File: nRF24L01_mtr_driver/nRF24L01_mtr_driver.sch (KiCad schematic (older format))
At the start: 135 parts, among them J1 Micro USB, J2 I/O, J4 VBAT, J5 MTR, J6 SERVO, J7 ICSP, Q1 AO4484, Q2 AO4484, Q3 AO4484, Q4 AO4484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

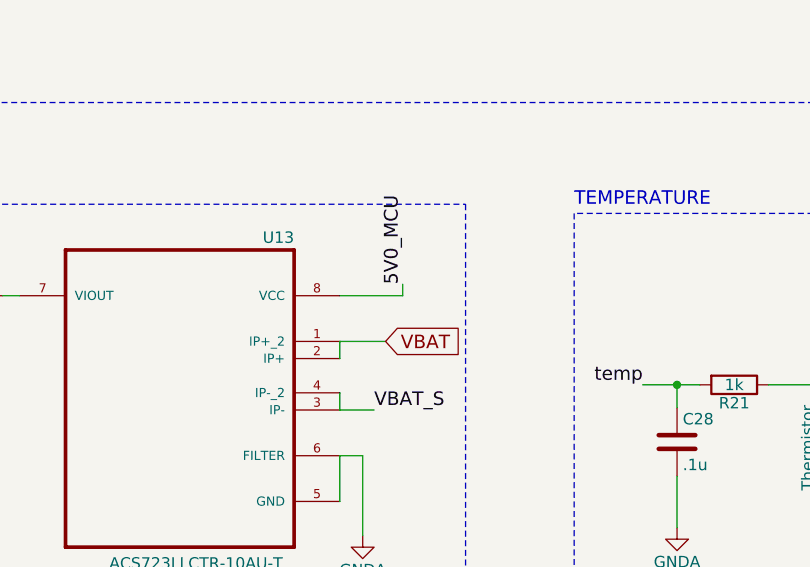
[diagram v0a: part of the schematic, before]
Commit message: 23 components left, stil needs routing
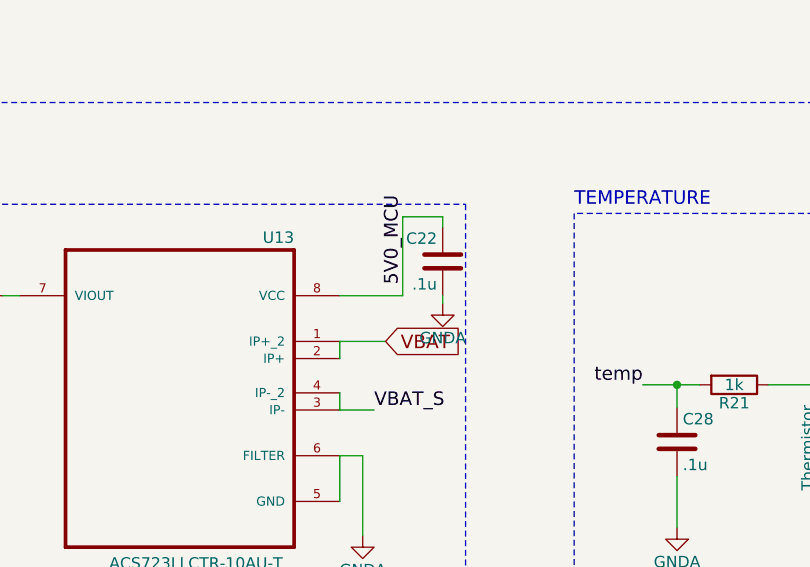
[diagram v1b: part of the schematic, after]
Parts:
- added C22: .1u, Capacitors_SMD:C_0402, symbol C
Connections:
- net 5V0_MCU: now also C22.1
- net GNDA: now also C22.2
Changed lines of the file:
@@
 	22630 9335 22630 8985
 Wire Wire Line
-	22805 8285 22805 8235
-Wire Wire Line
-	22530 8285 22805 8285
+	22805 7940 22805 8285
+Wire Wire Line
+	22805 8285 22530 8285
 Wire Wire Line
 	20590 12520 20665 12520
@@
 Text Notes 3750 6575 0    59   ~ 0
 F3542CT-ND
+$Comp
+L C C22
+U 1 1 5C739D0E
+P 22980 8135
+F 0 "C22" H 23005 8235 50  0000 L CNN
+F 1 ".1u" H 23005 8035 50  0000 L CNN
+F 2 "Capacitors_SMD:C_0402" H 23018 7985 50  0001 C CNN
+F 3 "" H 22980 8135 50  0001 C CNN
+	1    22980 8135
+	-1   0    0    -1
+$EndComp
+$Comp
+L GNDA #PWR081
+U 1 1 5C739D9E
+P 22980 8320
+F 0 "#PWR081" H 22980 8070 50  0001 C CNN
+F 1 "GNDA" H 22980 8170 50  0000 C CNN
+F 2 "" H 22980 8320 50  0001 C CNN
+F 3 "" H 22980 8320 50  0001 C CNN
+	1    22980 8320
+	-1   0    0    -1
+$EndComp
+Wire Wire Line
+	22980 8285 22980 8320
+Wire Wire Line
+	22805 7940 22980 7940
+Wire Wire Line
+	22980 7940 22980 7985
 $EndSCHEMATC

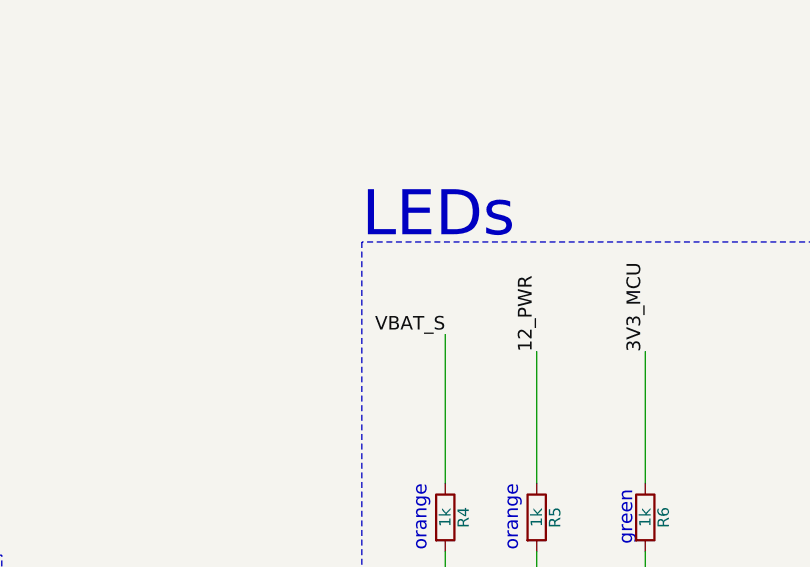
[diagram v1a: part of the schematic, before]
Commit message: arranged silkscreen, started rounting (ftdi)
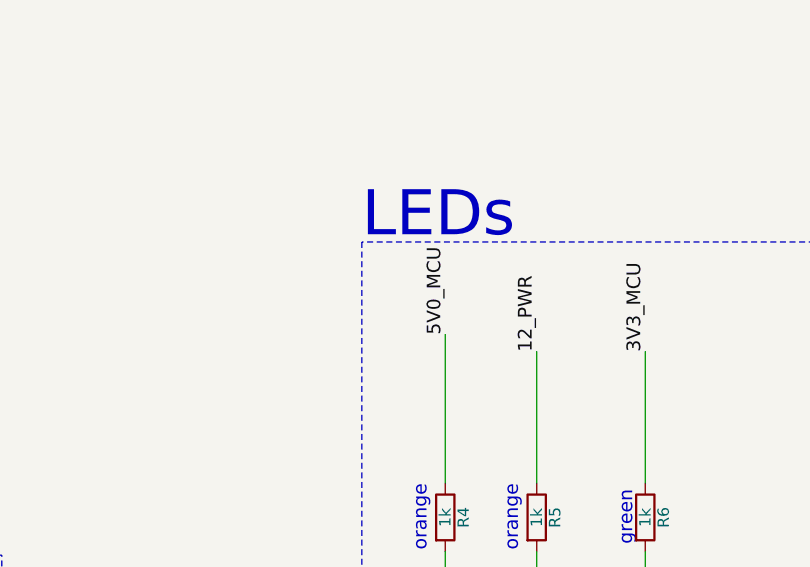
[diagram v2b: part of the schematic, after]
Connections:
- net 5V0_MCU: now also R4.1
- net VBAT_S: no longer R4.1
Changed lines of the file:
@@
 Text Label 9405 16400 1    60   ~ 0
 5V0_MCU
-Text Label 21735 2710 2    59   ~ 0
-VBAT_S
+Text Label 21735 2710 1    59   ~ 0
+5V0_MCU
 $Comp
 L LED D7

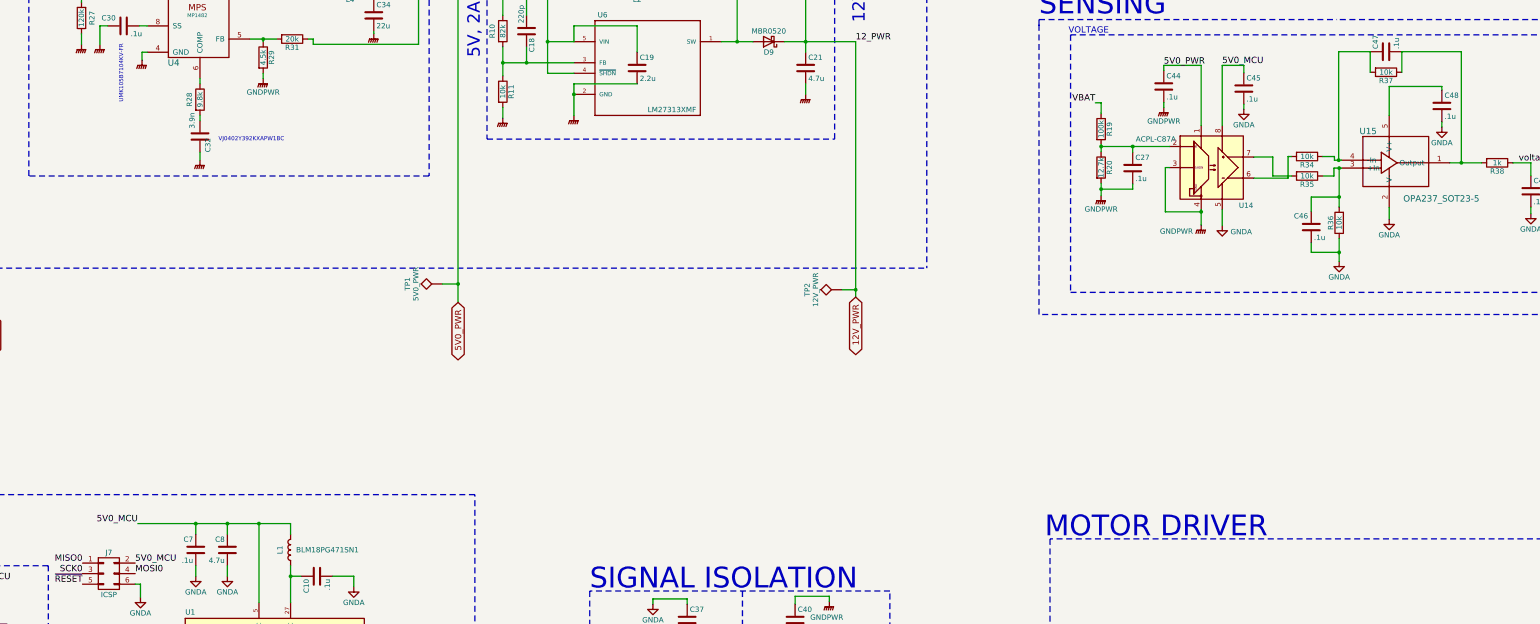
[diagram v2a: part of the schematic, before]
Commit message: ready for 2 or 4 layer implementation
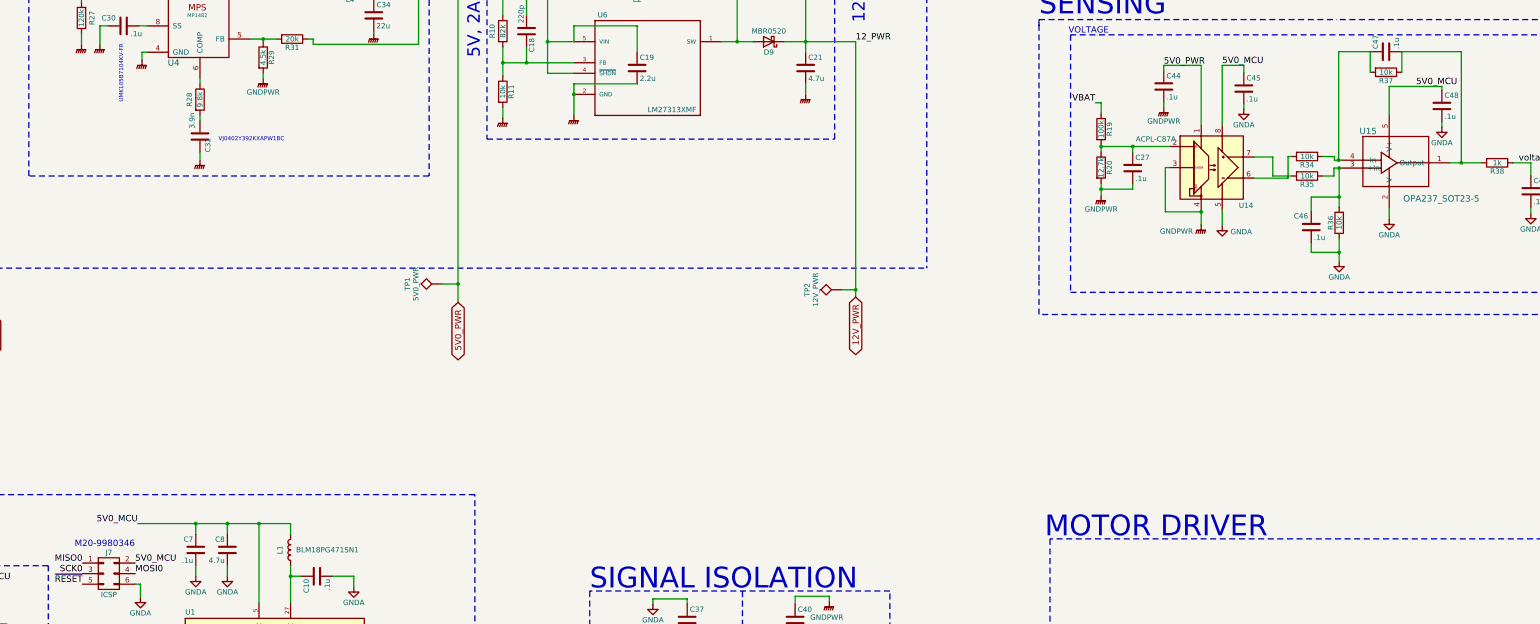
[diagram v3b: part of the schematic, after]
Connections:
- net ~SS1 is gone; now on net ~SS1~: J2.8 (Pin_8)
- net 5V0_MCU: now also C48.1, U15.5 (V+)
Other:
- note added: "M20-9980346"
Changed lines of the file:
@@
 Text Label 2015 14810 2    60   ~ 0
 SCK1
-Text Label 2515 14810 0    60   ~ 0
-~SS1
 Text Label 2515 14910 0    60   ~ 0
 MOSI1
@@
 Wire Wire Line
 	22980 7940 22980 7985
+Text Label 18490 8075 0    60   ~ 0
+5V0_MCU
+Text Label 2515 14810 0    60   ~ 0
+~SS1~
+Text Notes 5755 12455 0    60   ~ 0
+M20-9980346
 $EndSCHEMATC

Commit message: logic side rounting done (4 layer)
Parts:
- removed D7: LED, LEDs:LED_0603, symbol LED
- removed R23: 1k, Resistors_SMD:R_0402, symbol R
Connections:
- net 5V is gone; now on net 5V0_MCU: R22.1, R25.1
- net GNDA: no longer D2.1 (K), D4.1 (K)
- net GNDPWR: now also D2.1 (K), D4.1 (K)
- net LED2 renamed MOSI0
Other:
- note removed: "red"
- moved on the sheet: D2, D4, D6, R14, R5, R8

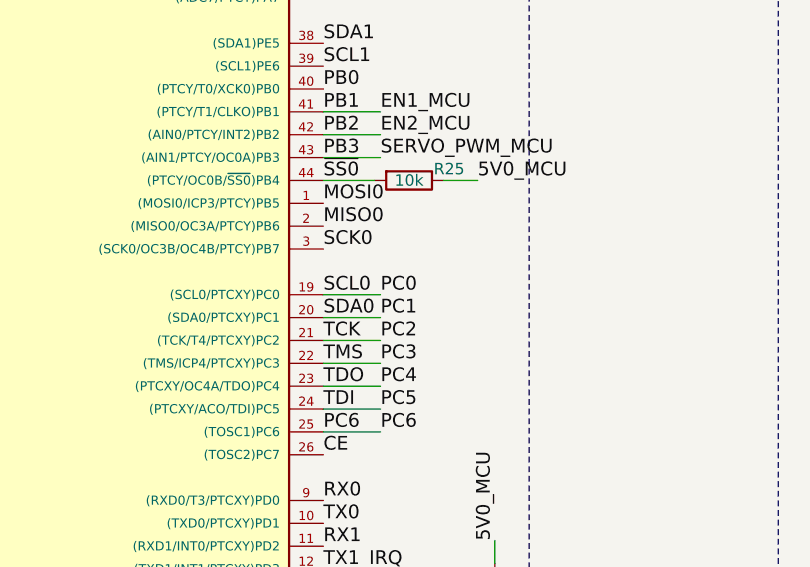
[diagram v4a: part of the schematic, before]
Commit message: added LED1
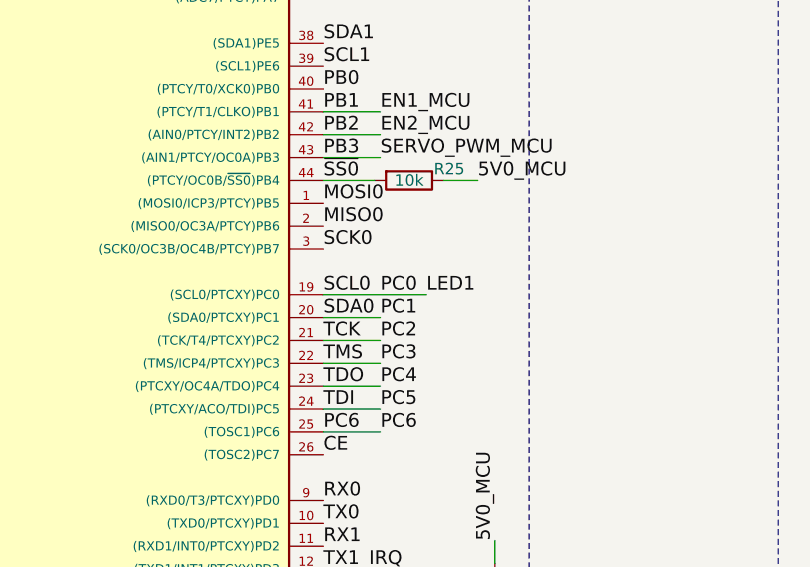
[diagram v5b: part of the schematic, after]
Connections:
- net PC0 is gone; now on net LED1: J2.20 (Pin_20), U1.19 ((SCL0/PTCXY)PC0)

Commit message: 4-layer, most of the routing done (logic + pwr)
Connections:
- net VBAT: no longer C14.1, C29.1, R19.1, R26.2, U4.2 (VIN)
- net VBAT_S: now also C14.1, C29.1, R19.1, R26.2, U4.2 (VIN)
- net SW: now reaches C33.1, L4.1, U4.3 (SW)
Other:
- moved on the sheet: C12, C13, C14, C16, C18, C19, C2, C21, C22, C23, C26, C27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

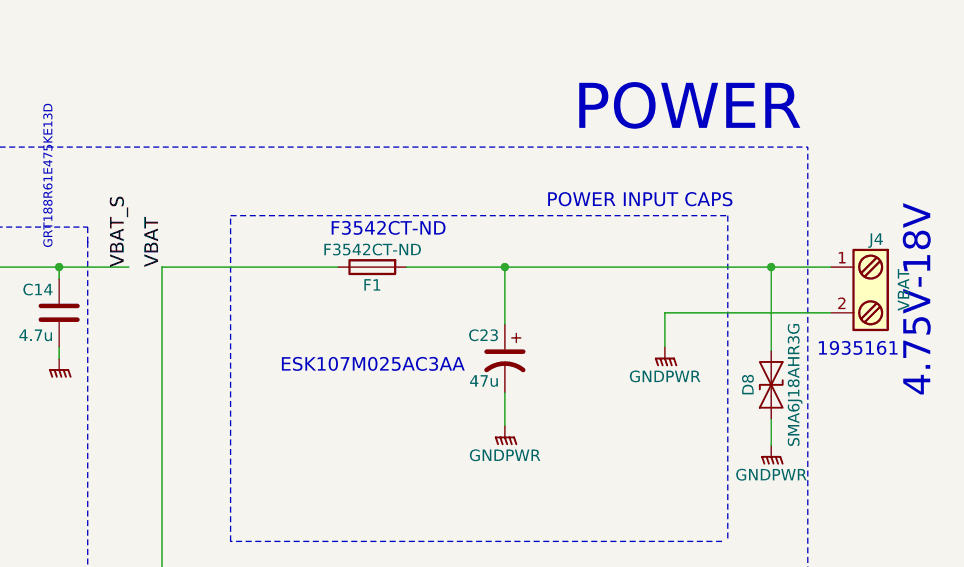
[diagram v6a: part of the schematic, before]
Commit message: All pour planes finalized
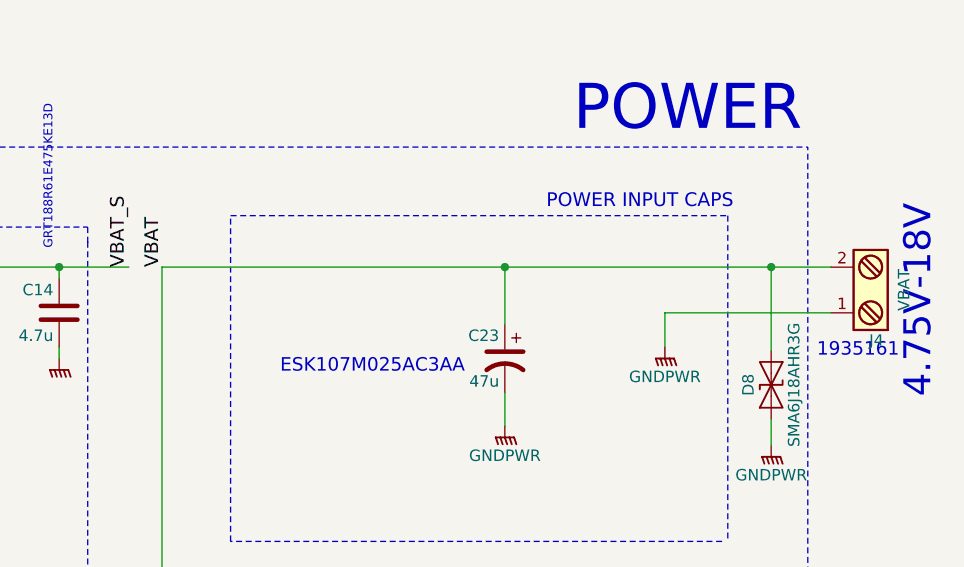
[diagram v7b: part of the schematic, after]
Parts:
- removed F1: F3542CT-ND, Resistors:1206, symbol Fuse
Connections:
- net GNDPWR: now also J4.1; no longer J4.2
- net VBAT: now also C23.1, D8.1 (A1), J4.2
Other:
- note removed: "F3542CT-ND"
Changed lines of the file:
@@
 F 3 "" H 25610 6890 50  0001 C CNN
 	1    25635 6890
-	-1   0    0    -1
+	-1   0    0    1
 $EndComp
 Text Notes 25735 7190 2    59   ~ 0
@@
 	-1   0    0    -1
 $EndComp
-$Comp
-L Fuse F1
-U 1 1 5C77D41B
-P 23430 6790
-F 0 "F1" V 23510 6790 50  0000 C CNN
-F 1 "F3542CT-ND" V 23355 6790 50  0000 C CNN
-F 2 "Resistors:1206" V 23360 6790 50  0001 C CNN
-F 3 "" H 23430 6790 50  0001 C CNN
-	1    23430 6790
-	0    -1   1    0
-$EndComp
 Text Label 8040 8890 2    60   ~ 0
 voltage
@@
 	25170 6790 25435 6790
 Wire Wire Line
-	23580 6790 25175 6790
-Text Notes 23755 6665 2    59   ~ 0
-F3542CT-ND
+	22510 6790 25175 6790
 $Comp
 L C C22
@@
 Wire Wire Line
 	20785 6790 22365 6790
-Wire Wire Line
-	22510 6790 23280 6790
 $EndSCHEMATC

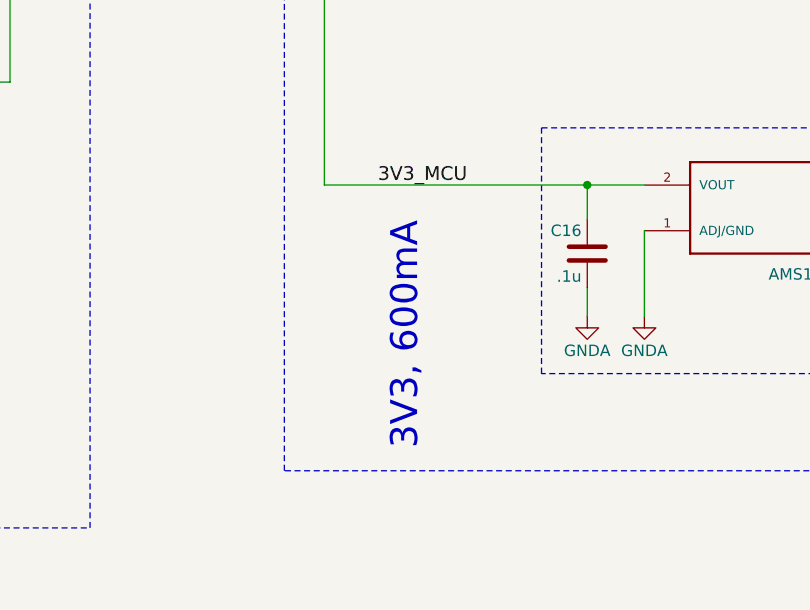
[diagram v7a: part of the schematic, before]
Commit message: silkscreen touch-up done, added AMS117 and Block Term 3D models
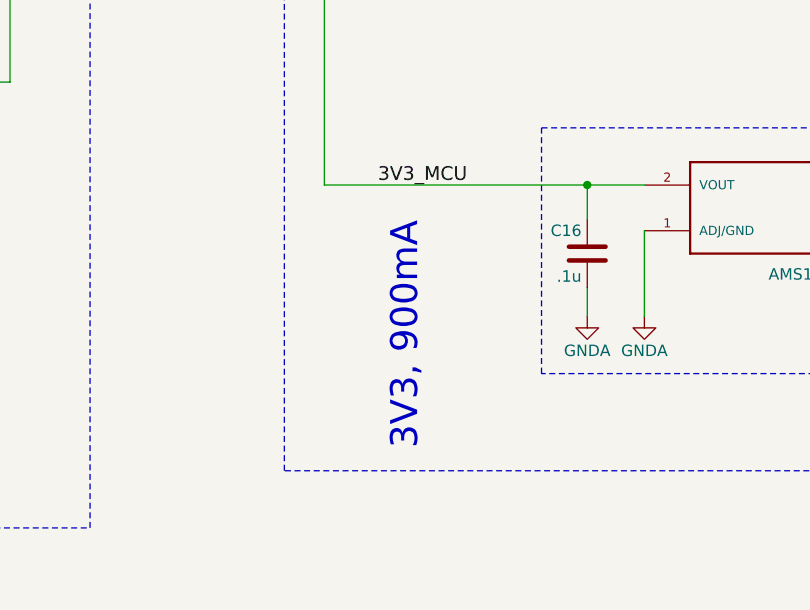
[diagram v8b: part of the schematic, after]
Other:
- note added: "3V3, 900mA\n"
- note removed: "3V3, 600mA\n"
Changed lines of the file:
@@
 5V, 600mA
 Text Notes 8305 5950 1    118  ~ 0
-3V3, 600mA\n
+3V3, 900mA\n
 Text Notes 17330 5275 1    118  ~ 0
 5V, 2A
